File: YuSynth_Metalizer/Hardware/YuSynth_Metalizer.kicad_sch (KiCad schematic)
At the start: 60 parts, among them Q1 BC547, Q10 BC547, Q11 BC557, Q12 BC547, Q2 BC547, Q5 BC557, Q6 BC547, Q7 BC557, Q8 BC547, Q9 BC557, U1 TL072, U2 TL074, U31 TL074, U37 TL074

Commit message: Done with YuSynth Metalizer schematic, starting with 6hp THT PCB
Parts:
- added C37, C38, C39, C40: 100n, Capacitor_THT:C_Rect_L7.0mm_W3.5mm_P5.00mm, symbol Device:C
- added C41, C42: 47uf, Capacitor_THT:CP_Radial_D6.3mm_P2.50mm, symbol Device:C_Polarized
- added J37: CV1, Connector_Audio:Jack_3.5mm_QingPu_WQP-PJ398SM_Vertical_CircularHoles, symbol Connector:AudioJack2
- added J38: CV2, Connector_Audio:Jack_3.5mm_QingPu_WQP-PJ398SM_Vertical_CircularHoles, symbol Connector:AudioJack2
- added Q3, Q4: BC547, Package_TO_SOT_THT:TO-92_Inline, symbol Transistor_BJT:BC547
- added R12, R13, R44: 270k, Resistor_THT:R_Axial_DIN0207_L6.3mm_D2.5mm_P7.62mm_Horizontal, symbol Device:R
- added R14: 150k, Resistor_THT:R_Axial_DIN0207_L6.3mm_D2.5mm_P7.62mm_Horizontal, symbol Device:R
- added R15: 10, Resistor_THT:R_Axial_DIN0207_L6.3mm_D2.5mm_P7.62mm_Horizontal, symbol Device:R
- added R16: 100k, Resistor_THT:R_Axial_DIN0207_L6.3mm_D2.5mm_P7.62mm_Horizontal, symbol Device:R
- added R17: 1.5k, Resistor_THT:R_Axial_DIN0207_L6.3mm_D2.5mm_P7.62mm_Horizontal, symbol Device:R
- added R43: 120k, Resistor_THT:R_Axial_DIN0207_L6.3mm_D2.5mm_P7.62mm_Horizontal, symbol Device:R
- added RV37: CV1, Potentiometer_THT:Potentiometer_Alpha_RD901F-40-00D_Single_Vertical, symbol Device:R_Potentiometer
- added RV38: CV2, Potentiometer_THT:Potentiometer_Alpha_RD901F-40-00D_Single_Vertical, symbol Device:R_Potentiometer
- added RV39: Shape, Potentiometer_THT:Potentiometer_Alpha_RD901F-40-00D_Single_Vertical, symbol Device:R_Potentiometer
- added unit 1 of U1
- added U37: ~, Connector_IDC:IDC-Header_2x05_P2.54mm_Vertical, symbol 1_Max_Eurorack:10pin_Header
- C10, C4, C6, C8: footprint (none) -> Capacitor_THT:C_Rect_L4.0mm_W2.5mm_P2.50mm
- C11: footprint (none) -> Capacitor_THT:CP_Radial_D6.3mm_P2.50mm
- C3, C5, C7, C9: footprint (none) -> Capacitor_THT:C_Rect_L7.0mm_W3.5mm_P5.00mm
- J39: renamed from J?; value AudioJack2 -> In; footprint (none) -> Connector_Audio:Jack_3.5mm_QingPu_WQP-PJ398SM_Vertical_CircularHoles
- J40: renamed from J?; value AudioJack2 -> Out; footprint (none) -> Connector_Audio:Jack_3.5mm_QingPu_WQP-PJ398SM_Vertical_CircularHoles
- R10, R11, R19, R20, R21, R22, R23, R24, R25, R26, R27, R28, R29, R3, R30, R31, R32, R33, R34, R35, R36, R37, R38, R39, R4, R40, R41, R42, R5, R7, R8, R9: footprint (none) -> Resistor_THT:R_Axial_DIN0207_L6.3mm_D2.5mm_P7.62mm_Horizontal
- U1: footprint (none) -> Package_DIP:DIP-8_W7.62mm_LongPads
- U1: renamed from U?; footprint (none) -> Package_DIP:DIP-8_W7.62mm_LongPads
- U2: footprint (none) -> Package_DIP:DIP-14_W7.62mm_LongPads
- U2: renamed from U31; footprint (none) -> Package_DIP:DIP-14_W7.62mm_LongPads
- U2: renamed from U?; footprint (none) -> Package_DIP:DIP-14_W7.62mm_LongPads
- U2: renamed from U37; footprint (none) -> Package_DIP:DIP-14_W7.62mm_LongPads
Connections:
- net +12V: now also C41.1, R43.1, RV39.1, U37. (GND)
- net GND: now also C37.1, C38.1, C39.2, C40.2, C41.2, C42.1, J37.S, J38.S, Q3.1 (C), Q4.2 (B), R17.2, RV37.3, RV38.3, RV39.3, U1.3 (+), U37. (GND); no longer R22.2, R28.2, R34.2, R40.2
- net at Q1.3 (E), Q2.3 (E): now also R15.1
- net at U2.11 (V-): now also C40.1
- net at U2.4 (V+): now also C37.2
- net at U1.4 (V-): now also C39.1
- net at U1.8 (V+): now also C38.2
- new net: J38.T, RV38.1
- new net: R12.1, RV38.2
- new net: R12.2, R13.2, R14.1, R44.2, U1.2 (-)
- new net: Q4.1 (C), R15.2
- new net: Q3.3 (E), Q4.3 (E)
- new net: J37.T, RV37.1
- new net: R13.1, RV39.2
- new net: Q3.2 (B), R16.2, R17.1, R43.2
- new net: R14.2, R16.1, U1.1
- new net: R44.1, RV37.2
- new net -12V: C42.2, R22.2, R28.2, R34.2, R40.2, U37. (GND)
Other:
- moved on the sheet: U1C, U2E

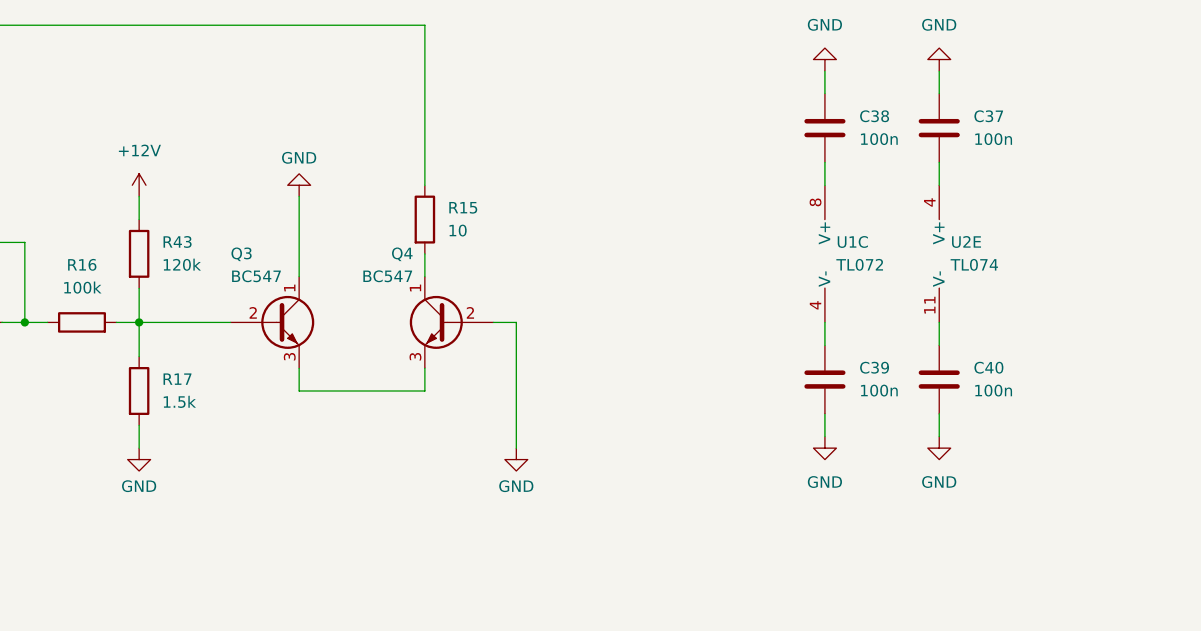
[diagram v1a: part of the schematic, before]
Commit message: Fixed OpAmp supply range error & redid PCB
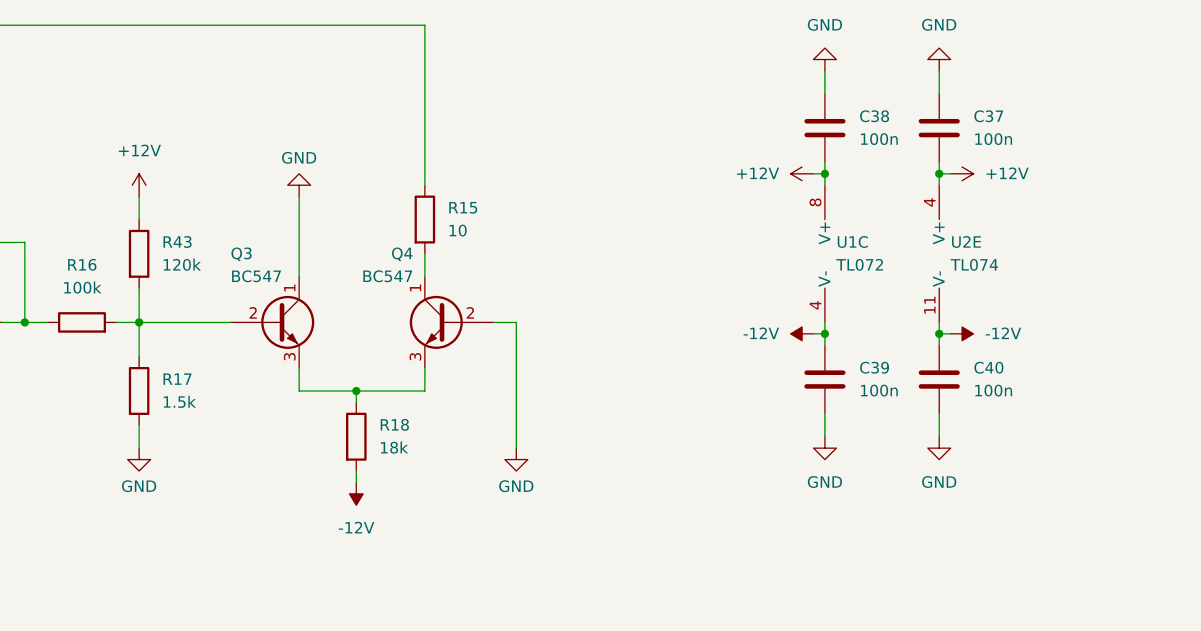
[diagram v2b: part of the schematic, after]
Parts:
- added R18: 18k, Resistor_THT:R_Axial_DIN0207_L6.3mm_D2.5mm_P7.62mm_Horizontal, symbol Device:R
- C37, C38, C39, C40: footprint Capacitor_THT:C_Rect_L7.0mm_W3.5mm_P5.00mm -> Capacitor_THT:C_Rect_L7.0mm_W2.0mm_P5.00mm
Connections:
- net +12V: now also C37.2, C38.2, U1.8 (V+), U2.4 (V+)
- net -12V: now also C39.1, C40.1, U1.4 (V-), U2.11 (V-), R18.2
- net at Q3.3 (E), Q4.3 (E): now also R18.1

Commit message: Main board & panel nearly done
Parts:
- removed U37: ~, Connector_IDC:IDC-Header_2x05_P2.54mm_Vertical, symbol 1_Max_Eurorack:10pin_Header
- added J41, J42, J43, J44: Conn_01x10, Connector_PinHeader_2.54mm:PinHeader_1x10_P2.54mm_Vertical, symbol Connector_Generic:Conn_01x10
- added J45: Conn_02x05_Odd_Even, Connector_IDC:IDC-Header_2x05_P2.54mm_Vertical, symbol Connector_Generic:Conn_02x05_Odd_Even
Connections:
- net +12V: now also J45.10 (Pin_10), J45.9 (Pin_9)
- net -12V: now also J45.1 (Pin_1), J45.2 (Pin_2)
- net GND: now also J45.3 (Pin_3), J45.4 (Pin_4), J45.5 (Pin_5), J45.6 (Pin_6), J45.7 (Pin_7), J45.8 (Pin_8)
